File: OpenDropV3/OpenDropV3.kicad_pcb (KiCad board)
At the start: 2 copper layers, 100 x 112 mm, 270 parts, among them J1 USB_C_Receptacle, J2 Conn_02x05_Odd_Even, P1 CONN_01X01, P10 CONN_01X01, P11 CONN_01X01, P12 CONN_01X01, P13 ScrewPad1, P14 ScrewPad2, P15 ScrewPad3, P16 ScrewPad4, P2 ScrewPad4, P3 CONN_01X01, P4 CONN_PSEUDO_AC, P7 CONN_01X01, P8 CONN_01X01, P9 CONN_01X01, SW1 SW_PUSH, SW2 SW_PUSH, SW3 SW_PUSH, SW5 SPST, T1 TK560P60Y, U1 MAX1771ESA, U10 AQY210EH, U11 AQY210EH, U12 AQY210EH, U13 AQY210EH, U14 TLV1117-33, U15 MCP41010, U16 74xx14, U2 HV507, U3 PAM8301, U4 HV507, U5 SAMD21G18B-A changed from SAM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, U6 MCP6002, U7 HCPL0534, U8 HCPL0534, U9 HCPL0534, Y1 32.765

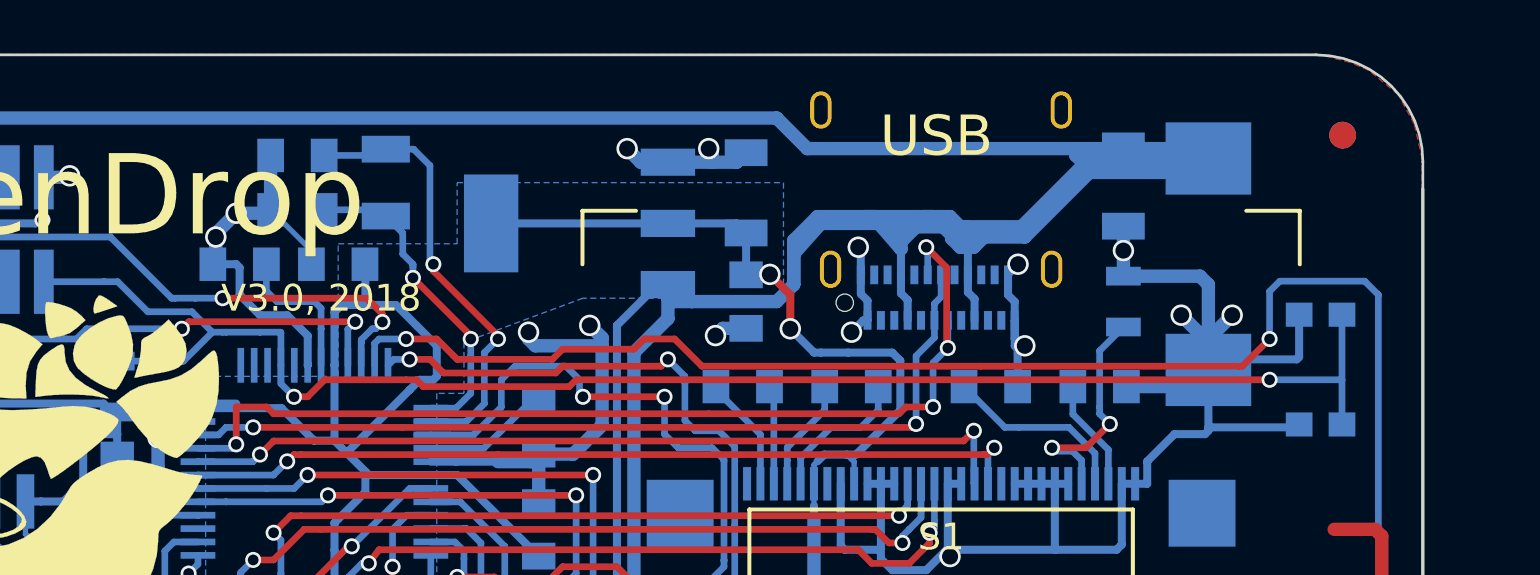
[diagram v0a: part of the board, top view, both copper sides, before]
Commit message: Add USB C pulldowns
Fixes #12
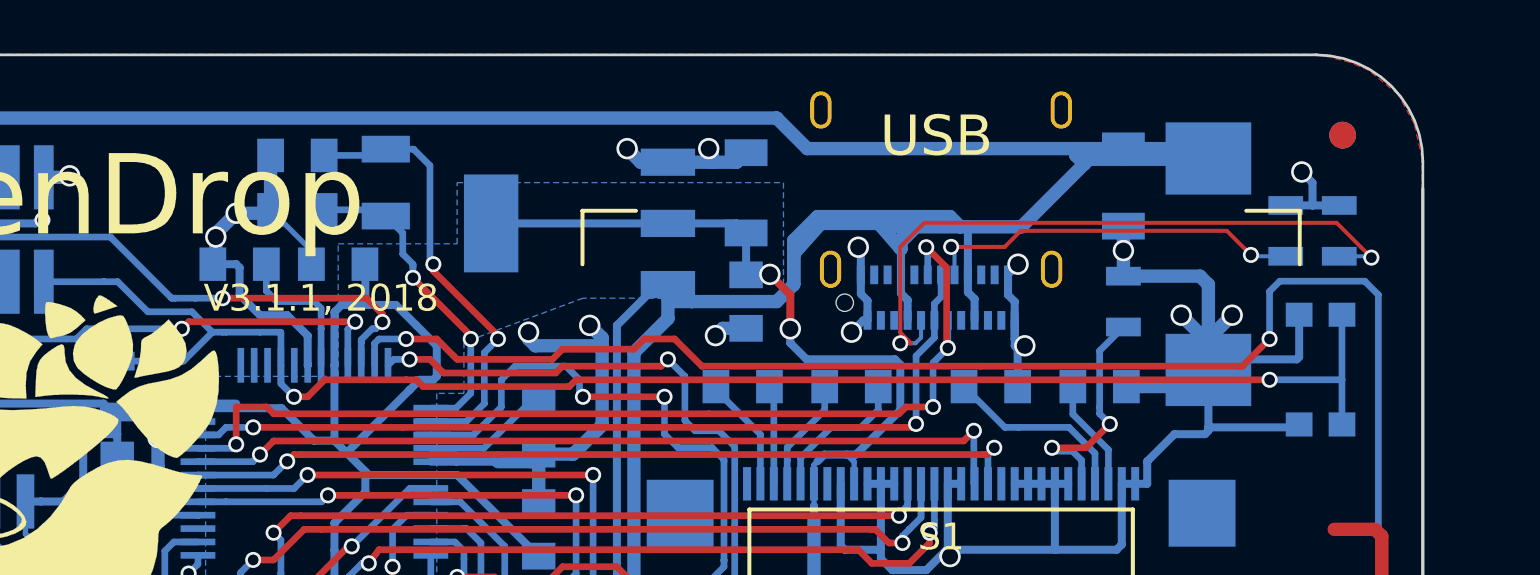
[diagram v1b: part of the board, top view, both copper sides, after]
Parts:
- added R14: 5.1k, Resistors_SMD:R_0805, B.Cu at (144.9, 37.6)
- added R23: 5.1k, Resistors_SMD:R_0805, B.Cu at (146.9, 37.6)
- C21, C5: value 10uF -> 22uF
- C32: value 100uF,35V -> 100uF,50V
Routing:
- net Net-(J1-PadA5): track 0.00 -> 25.4 mm, vias 0 -> 2
- net V_USB: track 302.4 -> 286.0 mm
- net Net-(J1-PadB5): track 0.00 -> 14.2 mm, vias 0 -> 2
- net GND: track 363.8 -> 367.2 mm, vias 49 -> 50
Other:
- board text added: "V3.1.1, 2018"
- board text removed: "V3.0, 2018"

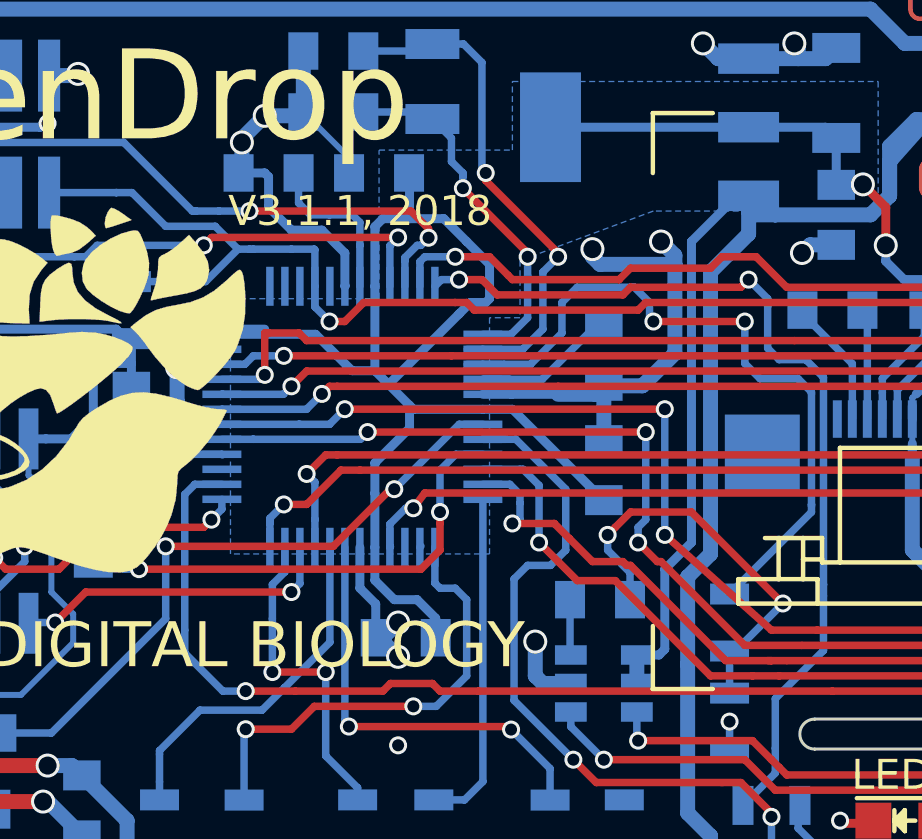
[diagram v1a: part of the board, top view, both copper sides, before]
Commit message: Connect speaker driver to 3.3V (instead of 5V)
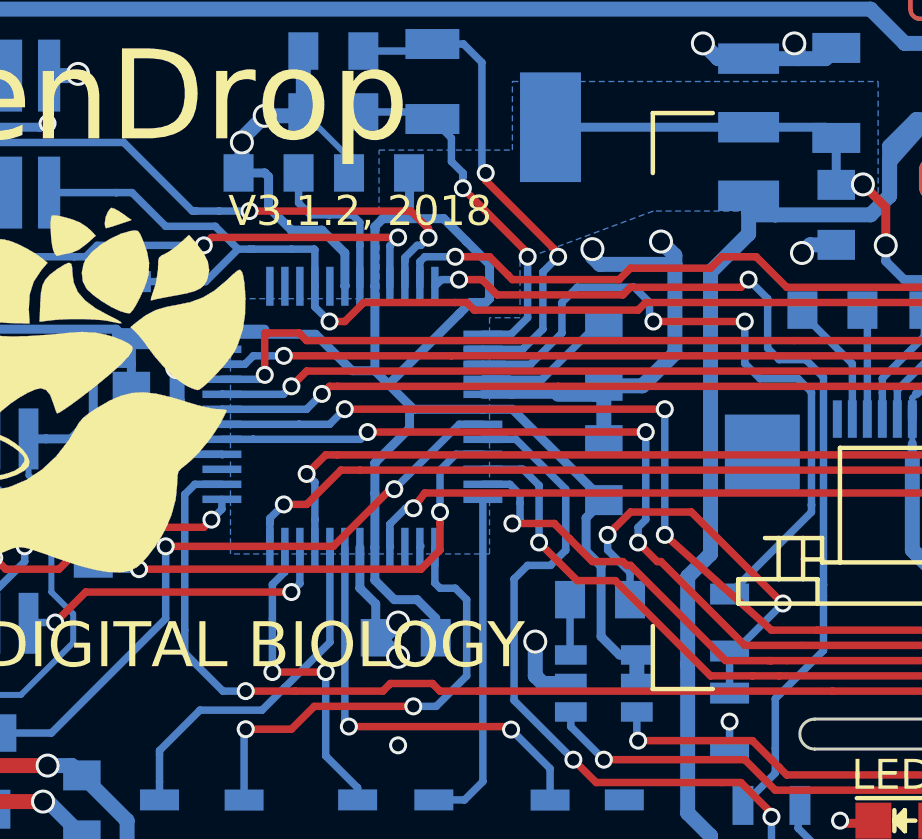
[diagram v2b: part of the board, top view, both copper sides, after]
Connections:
- U3 pad 4: V_USB -> +3V3
- U3 pad 5: V_USB -> +3V3
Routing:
- net V_USB: track 286.0 -> 267.7 mm
- net +3V3: track 308.3 -> 315.9 mm
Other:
- board text added: "V3.1.2, 2018"
- board text removed: "V3.1.1, 2018"
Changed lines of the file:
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@@
       (net 76 "Net-(C11-Pad2)"))
     (pad 4 smd rect (at 1.1 -0.95) (size 1.06 0.65) (layers B.Cu B.Paste B.Mask)
-      (net 250 V_USB))
+      (net 60 +3V3))
     (pad 6 smd rect (at 1.1 0.95) (size 1.06 0.65) (layers B.Cu B.Paste B.Mask)
       (net 86 "Net-(SP1-Pad2)"))
     (pad 5 smd rect (at 1.1 0) (size 1.06 0.65) (layers B.Cu B.Paste B.Mask)
-      (net 250 V_USB))
+      (net 60 +3V3))
     (model TO_SOT_Packages_SMD.3dshapes/SOT-23-6.wrl
       (at (xyz 0 0 0))
@@
     (effects (font (size 1.5 1.5) (thickness 0.3)))
   )
-  (gr_text "V3.1.1, 2018" (at 108.839 40.091) (layer F.SilkS)
+  (gr_text "V3.1.2, 2018" (at 108.839 40.091) (layer F.SilkS)
     (effects (font (size 1 1) (thickness 0.2)))
   )
@@
   (segment (start 54.4195 62.41015) (end 55.97635 63.967) (width 0.5) (layer B.Cu) (net 59))
   (segment (start 125.27 105.53) (end 125.24 105.5) (width 0.3) (layer B.Cu) (net 59) (status 30))
+  (segment (start 118.067 54.889) (end 117.489 54.889) (width 0.3) (layer B.Cu) (net 60))
+  (segment (start 116.375 50.319) (end 116.967 49.727) (width 0.3) (layer B.Cu) (net 60))
+  (segment (start 116.375 51.425598) (end 116.375 50.319) (width 0.3) (layer B.Cu) (net 60))
+  (segment (start 116.875 51.925598) (end 116.375 51.425598) (width 0.3) (layer B.Cu) (net 60))
+  (segment (start 116.875 54.275) (end 116.875 51.925598) (width 0.3) (layer B.Cu) (net 60))
+  (segment (start 117.489 54.889) (end 116.875 54.275) (width 0.3) (layer B.Cu) (net 60))
   (segment (start 126.365 41.234) (end 126.365 41.765) (width 0.3) (layer B.Cu) (net 60))
   (segment (start 125.587 39.218) (end 125.603 39.202) (width 0.3) (layer B.Cu) (net 60))
@@
   (segment (start 126.334 73.88704) (end 132.684 73.88704) (width 0.3) (layer B.Cu) (net 60))
   (segment (start 125.953 73.50604) (end 126.334 73.88704) (width 0.3) (layer B.Cu) (net 60))
+  (segment (start 118.067 54.889) (end 118.067 55.839) (width 0.5) (layer B.Cu) (net 60))
+  (segment (start 118.272 54.889) (end 118.067 54.889) (width 0.5) (layer B.Cu) (net 60))
   (segment (start 108.835 41.234) (end 108.835 40.468) (width 0.25) (layer B.Cu) (net 61))
   (segment (start 107.823 40.218) (end 107.188 40.218) (width 0.25) (layer B.Cu) (net 61))
@@
   (segment (start 119.761 55.204) (end 119.761 52.283) (width 0.5) (layer B.Cu) (net 250))
   (segment (start 119.761 52.283) (end 120.523 51.521) (width 0.5) (layer B.Cu) (net 250))
-  (segment (start 118.999 54.696) (end 118.999 52.029) (width 0.3) (layer B.Cu) (net 250))
-  (segment (start 118.999 52.029) (end 119.888 51.14) (width 0.3) (layer B.Cu) (net 250))
-  (segment (start 118.999 54.696) (end 118.806 54.889) (width 0.3) (layer B.Cu) (net 250))
   (segment (start 137.033 34.503) (end 137.033 34.757) (width 0.5) (layer B.Cu) (net 250))
   (segment (start 137.3505 35.0745) (end 137.3505 34.9) (width 0.5) (layer B.Cu) (net 250))
@@
   (segment (start 119.761 55.204) (end 119.761 60.157) (width 0.5) (layer B.Cu) (net 250))
   (segment (start 121.793 39.583) (end 121.412 39.583) (width 0.3) (layer B.Cu) (net 250))
-  (segment (start 121.412 39.583) (end 119.888 41.107) (width 0.3) (layer B.Cu) (net 250))
-  (segment (start 119.888 41.107) (end 119.888 51.14) (width 0.3) (layer B.Cu) (net 250))
-  (segment (start 118.806 54.889) (end 118.067 54.889) (width 0.3) (layer B.Cu) (net 250))
   (segment (start 133 39.22) (end 133 37.424) (width 0.3) (layer B.Cu) (net 250))
   (segment (start 132.969 37.551) (end 132.969 37.424) (width 0.3) (layer B.Cu) (net 250))
@@
   (segment (start 89.281 69.555) (end 89.281 67.523) (width 0.5) (layer B.Cu) (net 250))
   (segment (start 89.281 61.681) (end 89.281 60.411) (width 0.5) (layer F.Cu) (net 250))
-  (segment (start 118.067 54.889) (end 118.067 55.839) (width 0.5) (layer B.Cu) (net 250))
   (segment (start 89.2994 69.5734) (end 89.281 69.555) (width 0.5) (layer B.Cu) (net 250))
   (segment (start 90.69 69.5734) (end 89.2994 69.5734) (width 0.5) (layer B.Cu) (net 250))
@@
   (segment (start 74.095 75.143) (end 73.467 74.515) (width 0.5) (layer B.Cu) (net 250))
   (segment (start 73.467 74.515) (end 73.467 73.365) (width 0.5) (layer B.Cu) (net 250))
-  (segment (start 118.272 54.889) (end 118.067 54.889) (width 0.5) (layer B.Cu) (net 250))
   (segment (start 76.835 61.269) (end 76.883 61.317) (width 0.5) (layer B.Cu) (net 250))
   (segment (start 132.334 37.043) (end 132.715 37.424) (width 0.5) (layer B.Cu) (net 250))
